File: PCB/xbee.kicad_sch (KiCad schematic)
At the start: 5 parts

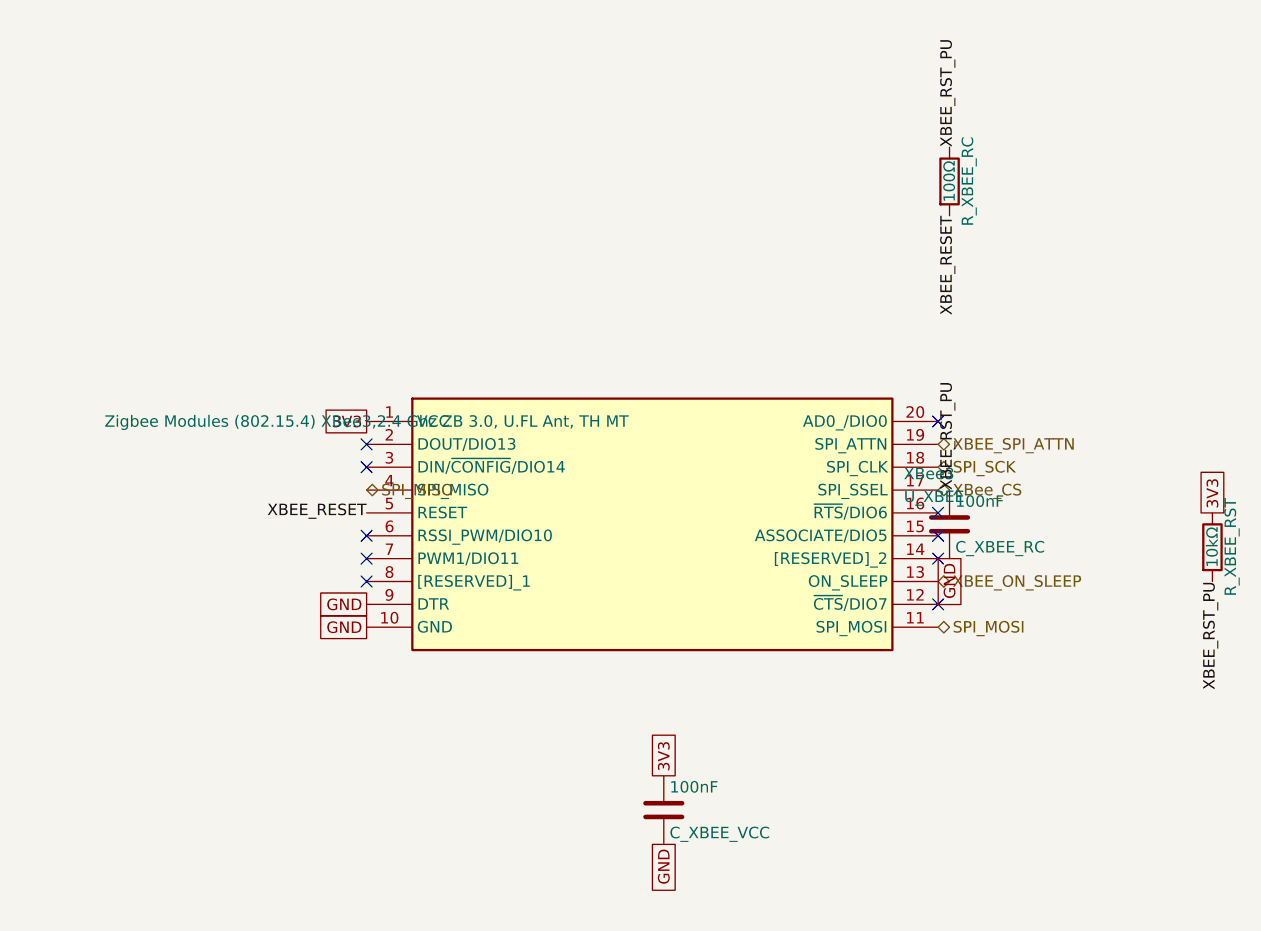
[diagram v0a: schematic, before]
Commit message: refactor: erc is clean
This gets the schematic as clean as it can be.
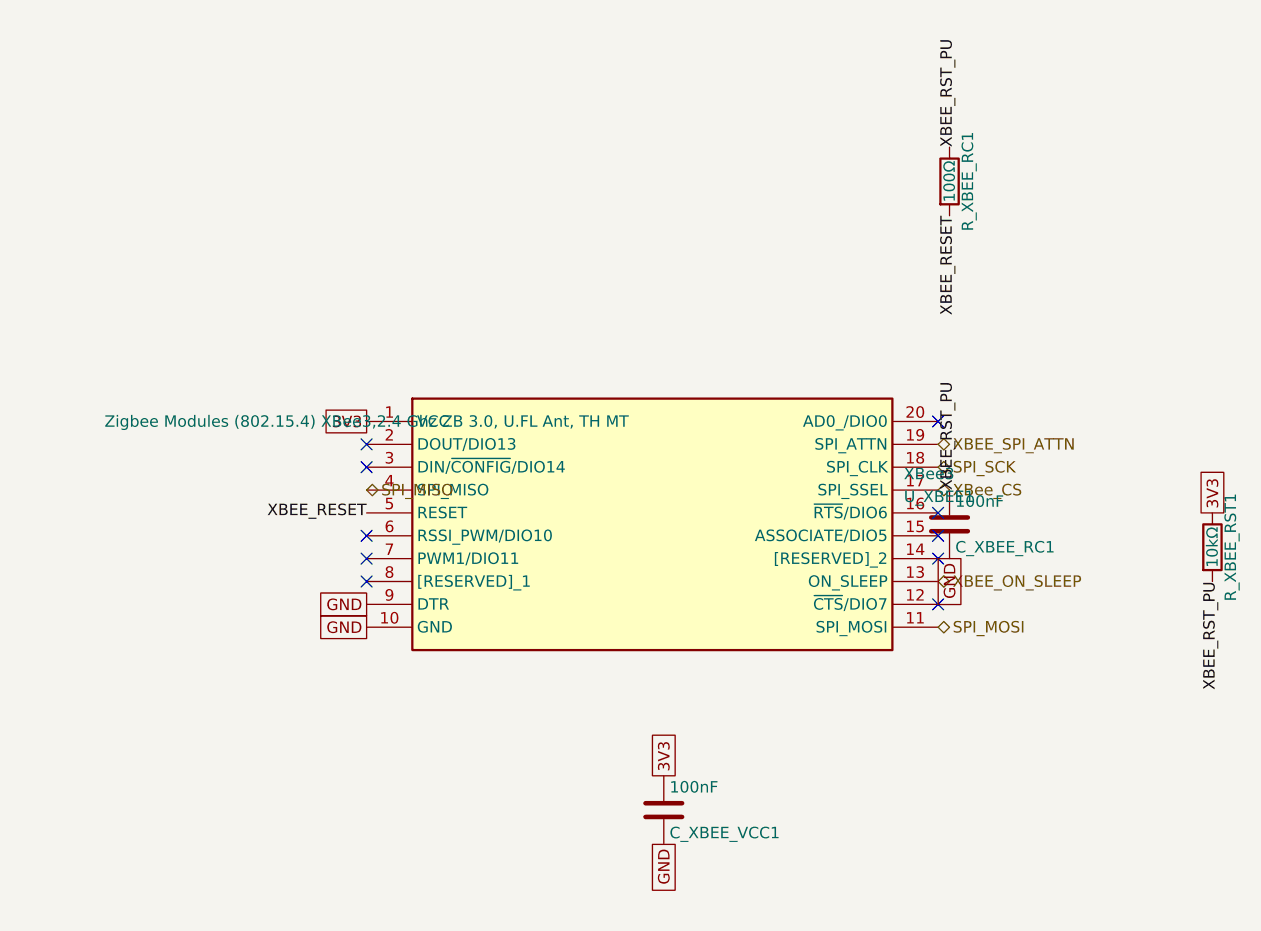
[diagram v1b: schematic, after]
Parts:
- removed C_XBEE_RC, C_XBEE_VCC: 100nF, symbol Device:C
- removed R_XBEE_RC: 100Ω, symbol Device:R
- removed R_XBEE_RST: 10kΩ, symbol Device:R
- removed U_XBEE: XBee3, symbol Xbee3:XB3-24Z8UT-J
- added C_XBEE_RC1, C_XBEE_VCC1: 100nF, symbol Device:C
- added R_XBEE_RC1: 100Ω, symbol Device:R
- added R_XBEE_RST1: 10kΩ, symbol Device:R
- added U_XBEE1: XBee3, symbol Xbee3:XB3-24Z8UT-J
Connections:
- net 3V3: now also C_XBEE_VCC1.1, R_XBEE_RST1.1, U_XBEE1.1 (VCC)
- net GND: now also C_XBEE_RC1.2, C_XBEE_VCC1.2, U_XBEE1.10 (GND), U_XBEE1.9 (DTR)
- net SPI_MISO: now also U_XBEE1.4 (SPI_MISO)
- net SPI_MOSI: now also U_XBEE1.11 (SPI_MOSI)
- net SPI_SCK: now also U_XBEE1.18 (SPI_CLK)
- net XBEE_ON_SLEEP: now also U_XBEE1.13 (ON_SLEEP)
- net XBEE_RESET: now also R_XBEE_RC1.2, U_XBEE1.5 (RESET)
- net XBEE_RST_PU: now also C_XBEE_RC1.1, R_XBEE_RC1.1, R_XBEE_RST1.2
- net XBEE_SPI_ATTN: now also U_XBEE1.19 (SPI_ATTN)
- net XBee_CS: now also U_XBEE1.17 (SPI_SSEL)

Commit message: refactor: switch over to esp32-s3-wroom1 (#13)
This refactors to the esp32-s3 to avoid every problem we encountered with the raspberry pi options.
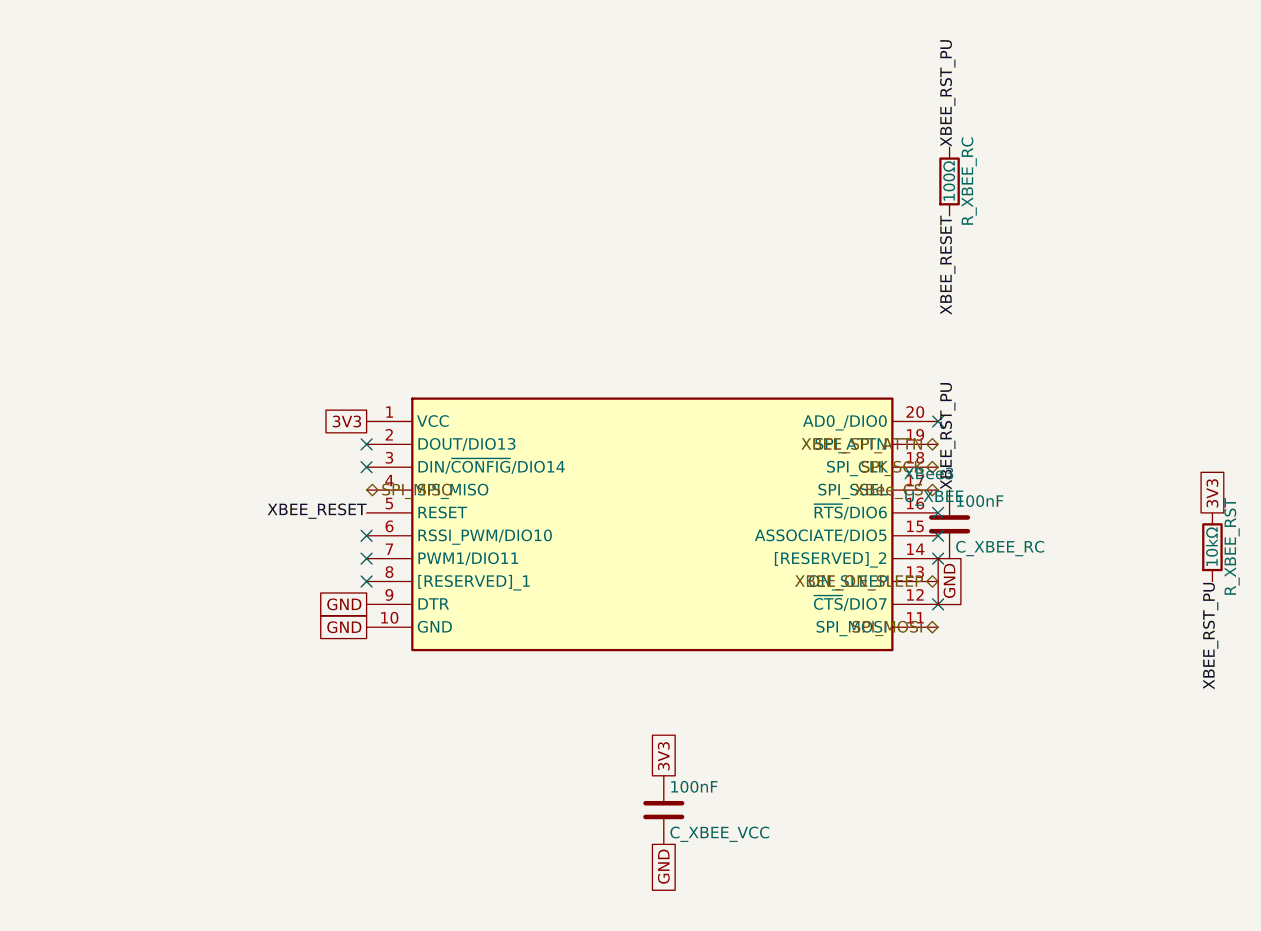
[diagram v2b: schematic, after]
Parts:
- removed C_XBEE_RC1, C_XBEE_VCC1: 100nF, symbol Device:C
- removed R_XBEE_RC1: 100Ω, symbol Device:R
- removed R_XBEE_RST1: 10kΩ, symbol Device:R
- removed U_XBEE1: XBee3, symbol Xbee3:XB3-24Z8UT-J
- added C_XBEE_RC, C_XBEE_VCC: 100nF, Capacitor_SMD:C_0402_1005Metric, symbol Device:C
- added R_XBEE_RC: 100Ω, Resistor_SMD:R_0402_1005Metric, symbol Device:R
- added R_XBEE_RST: 10kΩ, Resistor_SMD:R_0402_1005Metric, symbol Device:R
- added U_XBEE: XBee3, Xbee3:XB324Z8UTJ, symbol Xbee3:XB3-24Z8UT-J
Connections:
- net 3V3: now also C_XBEE_VCC.1, R_XBEE_RST.1, U_XBEE.1 (VCC)
- net GND: now also C_XBEE_RC.2, C_XBEE_VCC.2, U_XBEE.10 (GND), U_XBEE.9 (DTR)
- net SPI_MISO: now also U_XBEE.4 (SPI_MISO)
- net SPI_MOSI: now also U_XBEE.11 (SPI_MOSI)
- net SPI_SCK: now also U_XBEE.18 (SPI_CLK)
- net XBEE_ON_SLEEP: now also U_XBEE.13 (ON_SLEEP)
- net XBEE_RESET: now also R_XBEE_RC.2, U_XBEE.5 (RESET)
- net XBEE_RST_PU: now also C_XBEE_RC.1, R_XBEE_RC.1, R_XBEE_RST.2
- net XBEE_SPI_ATTN: now also U_XBEE.19 (SPI_ATTN)
- net XBee_CS: now also U_XBEE.17 (SPI_SSEL)

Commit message: cleanup: annotations and library updates
This is just a task to update the kicad libraries and annotations internally to get that clean ERC.
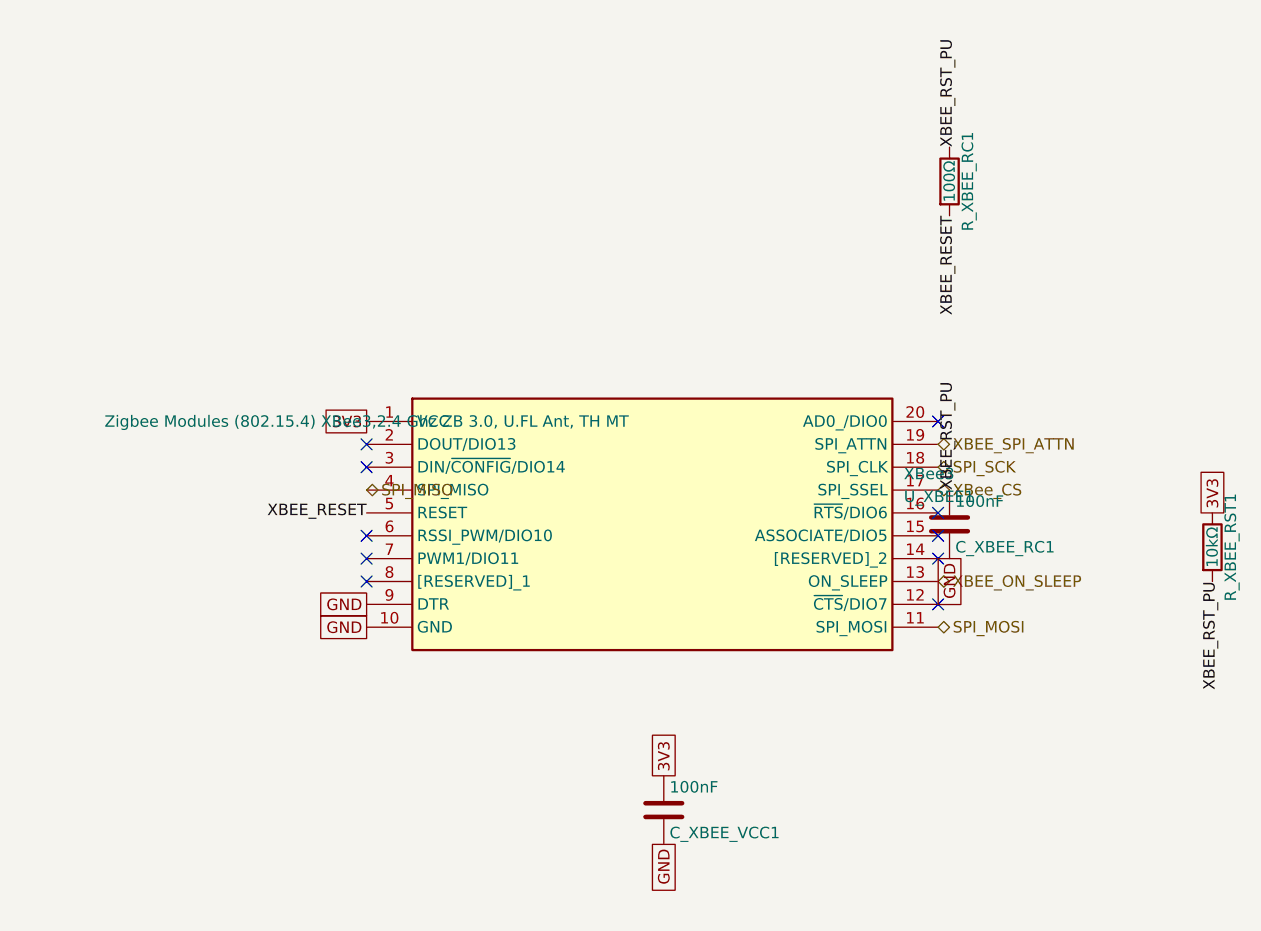
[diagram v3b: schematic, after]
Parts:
- renumbered C_XBEE_RC to C_XBEE_RC1, C_XBEE_VCC to C_XBEE_VCC1, R_XBEE_RC to R_XBEE_RC1, R_XBEE_RST to R_XBEE_RST1, U_XBEE to U_XBEE1
